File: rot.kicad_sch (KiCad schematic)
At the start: 35 parts, among them J4 PinSocket_2x6_P2.54mm_Drill1.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, J8 Plug_Molex_SlimStack_2x25_529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, U2 W25Q32JW_SOIC-8, U3 W25Q32JW_SOIC-8, U4 W25Q32JW_SOIC-8, U5 W25Q32JW_SOIC-8

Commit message: a lot of routing and almost all caps of the fpga are placed down
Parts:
- C35, C36, C37, C38: footprint antmicro-footprints:C_0402_1005Metric -> Capacitor_SMD:C_0402_1005Metric
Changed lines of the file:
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@@
 			)
 		)
-		(property "Footprint" "antmicro-footprints:C_0402_1005Metric"
+		(property "Footprint" "Capacitor_SMD:C_0402_1005Metric"
 			(at 125.73 48.26 0)
 			(hide yes)
@@
 			)
 		)
-		(property "Footprint" "antmicro-footprints:C_0402_1005Metric"
+		(property "Footprint" "Capacitor_SMD:C_0402_1005Metric"
 			(at 125.73 92.71 0)
 			(hide yes)
@@
 			)
 		)
-		(property "Footprint" "antmicro-footprints:C_0402_1005Metric"
+		(property "Footprint" "Capacitor_SMD:C_0402_1005Metric"
 			(at 125.73 168.91 0)
 			(hide yes)
@@
 			)
 		)
-		(property "Footprint" "antmicro-footprints:C_0402_1005Metric"
+		(property "Footprint" "Capacitor_SMD:C_0402_1005Metric"
 			(at 125.73 219.71 0)
 			(hide yes)

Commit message: a lot of poin swaps
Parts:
- C35, C36, C37, C38: MPN C1005X5R1E474M050BB -> GXT155C80J474KE01D; Manufacturer TDK -> Murata Electronics
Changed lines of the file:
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@@
 			)
 		)
-		(property "Datasheet" "https://product.tdk.com/en/search/capacitor/ceramic/mlcc/info?part_no=C1005X5R1E474M050BB"
+		(property "Datasheet" ""
 			(at 128.27 48.26 0)
 			(hide yes)
@@
 			)
 		)
-		(property "Description" "SMD Multilayer Ceramic Capacitor, 0.47 µF, 25 V, 0402 [1005 Metric], ± 20%, X5R, C"
+		(property "Description" "Multilayer Ceramic Capacitors MLCC - SMD/SMT 0402 6.3VDC 0.47uF 10% X6S AEC-Q200"
 			(at 113.03 68.58 0)
 			(hide yes)
@@
 			)
 		)
-		(property "Manufacturer" "TDK"
+		(property "Manufacturer" "Murata Electronics"
 			(at 133.35 48.26 0)
 			(hide yes)
@@
 			)
 		)
-		(property "MPN" "C1005X5R1E474M050BB"
+		(property "MPN" "GXT155C80J474KE01D"
 			(at 130.81 48.26 0)
 			(hide yes)
@@
 			)
 		)
-		(property "Datasheet" "https://product.tdk.com/en/search/capacitor/ceramic/mlcc/info?part_no=C1005X5R1E474M050BB"
+		(property "Datasheet" ""
 			(at 128.27 92.71 0)
 			(hide yes)
@@
 			)
 		)
-		(property "Description" "SMD Multilayer Ceramic Capacitor, 0.47 µF, 25 V, 0402 [1005 Metric], ± 20%, X5R, C"
+		(property "Description" "Multilayer Ceramic Capacitors MLCC - SMD/SMT 0402 6.3VDC 0.47uF 10% X6S AEC-Q200"
 			(at 113.03 113.03 0)
 			(hide yes)
@@
 			)
 		)
-		(property "Manufacturer" "TDK"
+		(property "Manufacturer" "Murata Electronics"
 			(at 133.35 92.71 0)
 			(hide yes)
@@
 			)
 		)
-		(property "MPN" "C1005X5R1E474M050BB"
+		(property "MPN" "GXT155C80J474KE01D"
 			(at 130.81 92.71 0)
 			(hide yes)
@@
 			)
 		)
-		(property "Datasheet" "https://product.tdk.com/en/search/capacitor/ceramic/mlcc/info?part_no=C1005X5R1E474M050BB"
+		(property "Datasheet" ""
 			(at 128.27 168.91 0)
 			(hide yes)
@@
 			)
 		)
-		(property "Description" "SMD Multilayer Ceramic Capacitor, 0.47 µF, 25 V, 0402 [1005 Metric], ± 20%, X5R, C"
+		(property "Description" "Multilayer Ceramic Capacitors MLCC - SMD/SMT 0402 6.3VDC 0.47uF 10% X6S AEC-Q200"
 			(at 113.03 189.23 0)
 			(hide yes)
@@
 			)
 		)
-		(property "Manufacturer" "TDK"
+		(property "Manufacturer" "Murata Electronics"
 			(at 133.35 168.91 0)
 			(hide yes)
@@
 			)
 		)
-		(property "MPN" "C1005X5R1E474M050BB"
+		(property "MPN" "GXT155C80J474KE01D"
 			(at 130.81 168.91 0)
 			(hide yes)
@@
 			)
 		)
-		(property "Datasheet" "https://product.tdk.com/en/search/capacitor/ceramic/mlcc/info?part_no=C1005X5R1E474M050BB"
+		(property "Datasheet" ""
 			(at 128.27 219.71 0)
 			(hide yes)
@@
 			)
 		)
-		(property "Description" "SMD Multilayer Ceramic Capacitor, 0.47 µF, 25 V, 0402 [1005 Metric], ± 20%, X5R, C"
+		(property "Description" "Multilayer Ceramic Capacitors MLCC - SMD/SMT 0402 6.3VDC 0.47uF 10% X6S AEC-Q200"
 			(at 113.03 240.03 0)
 			(hide yes)
@@
 			)
 		)
-		(property "Manufacturer" "TDK"
+		(property "Manufacturer" "Murata Electronics"
 			(at 133.35 219.71 0)
 			(hide yes)
@@
 			)
 		)
-		(property "MPN" "C1005X5R1E474M050BB"
+		(property "MPN" "GXT155C80J474KE01D"
 			(at 130.81 219.71 0)
 			(hide yes)

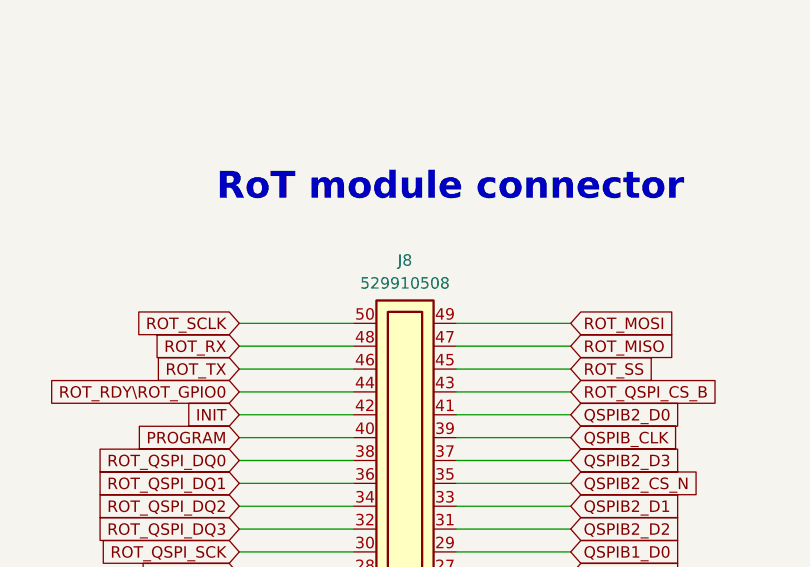
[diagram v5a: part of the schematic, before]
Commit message: bom changes
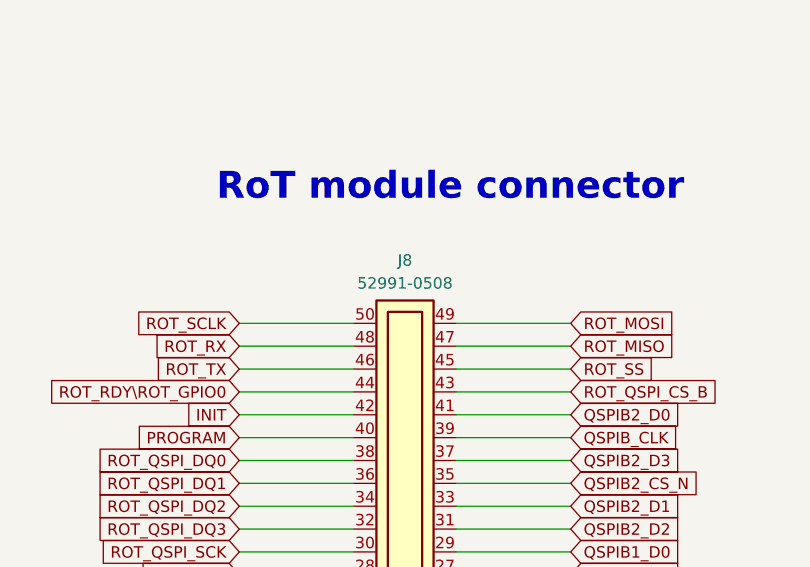
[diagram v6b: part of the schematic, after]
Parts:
- J8: MPN 529910508 -> 52991-0508; Pitch (none) -> 0.5 mm; Pitch  0.5 mm -> (none)

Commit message: version 1.0 complete
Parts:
- R21, R22, R23, R24: MPN CR0402-FX-4701GLF -> RC0402FR-7D4K7L; Manufacturer Bourns -> YAGEO
- R29, R30, R31, R32, R33, R34, R35, R36, R37, R38, R39, R40, R41, R42, R43, R44: MPN CR0402-FX-1002GLF -> CR0402AFX-1002GAS

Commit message: "In the process of upgrading the ddr memory"
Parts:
- removed C35, C36, C38: C_470n_0402, Capacitor_SMD:C_0402_1005Metric, symbol antmicroCapacitors0402:C_470n_0402
- removed H2: Spacer_Drill3.7mm_H4mm_9774040151R, antmicro-footprints:Spacer_Drill3.7mm_H4mm_9774040151R, symbol antmicroMechanicalParts:Spacer_Drill3.7mm_H4mm_9774040151R
- removed J4: PinSocket_2x6_P2.54mm_Drill1.02mm_PMOD, antmicro-footprints:PinSocket_2x6_P2.54mm_Drill1.02mm_PMOD, symbol antmicroGenericPinSockets:PinSocket_2x6_P2.54mm_Drill1.02mm_PMOD
- removed J8: Plug_Molex_SlimStack_2x25_529910508, antmicro-footprints:Conn_Plug_Molex_SlimStack_2x25_529910508, symbol antmicroB2BConnectors:Plug_Molex_SlimStack_2x25_529910508
- removed R21, R22, R24: R_4k7_0402, antmicro-footprints:R_0402_1005Metric, symbol antmicroResistors0402:R_4k7_0402
- removed R25, R26, R28: R_1k_0402, antmicro-footprints:R_0402_1005Metric, symbol antmicroResistors0402:R_1k_0402
- removed R29, R30, R32, R33, R34, R36, R37, R38, R40, R41, R42, R44: R_10k_0402, antmicro-footprints:R_0402_1005Metric, symbol antmicroResistors0402:R_10k_0402
- removed U2, U3, U5: W25Q32JW_SOIC-8, antmicro-footprints:SOIC-8_5.3x5.3x2mm_P1.27mm, symbol antmicroMemory:W25Q32JW_SOIC-8
- added IC3: IS25LP128F-JKLA3, SON127P600X500X80-9N-D, symbol artix-dc-scm:IS25LP128F-JKLA3
- R23, R27, R31, R35, R39, R43: footprint antmicro-footprints:R_0402_1005Metric -> Resistor_SMD:R_0402_1005Metric
- U4: now not fitted; now left out of the parts list
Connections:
- net GND: now also IC3.[4,9] (GND); no longer U4.4 (VSS)
- net VCC3V3: now also IC3.8 (VCC); no longer U4.8 (VCC)
- net QSPIA2_CS_N: no longer names the net of U4.1 (~{CS})
- net QSPIA2_CS_N: no longer R23.2
- net QSPIA2_D0: no longer names the net of U4.5 (SI/IO0)
- net QSPIA2_D0: no longer R31.1
- net QSPIA2_D1: no longer names the net of U4.2 (SO/IO1)
- net QSPIA2_D1: no longer R43.1
- net QSPIA2_D2: no longer names the net of U4.3 (~{WP}/IO2)
- net QSPIA2_D2: no longer R35.1
- net QSPIA2_D3: no longer names the net of U4.7 (~{HOLD}/IO3)
- net QSPIA2_D3: no longer R39.1
- net QSPIA_CLK: no longer names the net of U4.6 (SCLK)
- net QSPIA_CLK: no longer R27.2
- new net QSPI_CLK: IC3.6 (SCK), R27.2
- new net QSPI_CS_N: IC3.1 (CE#), R23.2
- new net QSPI_D0: IC3.5 (SI_(IO0)), R31.1
- new net QSPI_D1: IC3.2 (SO_(IO1)), R43.1
- new net QSPI_D2: IC3.3 (WP#_(IO2)), R35.1
- new net QSPI_D3: IC3.7 (HOLD_#_OR_RESET_#(IO3)), R39.1
- no-connect marks 1 -> 0
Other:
- note removed: "BIOS flash"
- note removed: "BMC flash"
- note removed: "One or typically two flash devices used to contain the BIOS firmware image"
- note removed: "One or typically two flash devices used to contain the BMC firmware image"
- note removed: "Pinout for AES-PMOD-TPM20-SLB9670-G"
- note removed: "RoT module connector"
- note removed: "TPM connector"
- note removed: "preliminary"
- moved on the sheet: C37
